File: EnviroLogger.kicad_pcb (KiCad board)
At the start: 2 copper layers, 100 x 99.5 mm, 30 parts, among them J3 Conn_01x03_Male, J4 Conn_01x02_Male, J5 Conn_01x02_Male, M1 RobotDyn_Li-Ion_Charger_W-Pro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, M2 MT3608_Boost_Regulator, M3 RobotDyn_MicroSD_Card_Reader, Q1 BSS138, Q2 BSS138, Q3 BSS138, SW1 SW_SPST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

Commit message: Updated to V1.1.0
Fixed many issues:
- Battery polarity was reversed
- I2C SDA and SCL were on the wrong Nano pins
- Added missing pull-up resistor on 5V side of I2C level shifter
- Added a real time clock to the design
- Fixed boost regulator wiring
- Changed MQ-135 control MOSFET to a part with much lower Rds(on) value.
The original part was dropping almost 25% as much voltage as the sensor
itself.
- Changed MQ-135 control to low-side switch design
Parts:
- removed J4, J5: Conn_01x02_Male, Connector_JST:JST_PH_S2B-PH-K_1x02_P2.00mm_Horizontal
- added BT1: Battery_Cell, Battery:BatteryHolder_Keystone_3000_1x12mm, F.Cu at (104.2, 132.5)
- added J1: Conn_01x02_Male, Connector_JST:JST_PH_S2B-PH-K_1x02_P2.00mm_Horizontal, F.Cu at (82.5, 112.5)
- added J2: Conn_01x02_Male, Connector_JST:JST_PH_S2B-PH-K_1x02_P2.00mm_Horizontal, F.Cu at (90.0, 112.5)
- added R10: 10k, Resistor_THT:R_Axial_DIN0207_L6.3mm_D2.5mm_P7.62mm_Horizontal, F.Cu at (43.5, 147.5)
- added R8: 10k, Resistor_THT:R_Axial_DIN0207_L6.3mm_D2.5mm_P7.62mm_Horizontal, F.Cu at (49.5, 147.5)
- added R9: 10k, Resistor_THT:R_Axial_DIN0207_L6.3mm_D2.5mm_P7.62mm_Horizontal, F.Cu at (46.5, 147.5)
- added U4: DS1307ZN+, Package_SO:SOIC-8_3.9x4.9mm_P1.27mm, F.Cu at (85.0, 163.8)
- added Y1: Crystal_GND23, Crystal:Crystal_SMD_CardinalComponents_CPFB-4Pin_8.7x3.7mm, F.Cu at (76.0, 163.8)
- Q1: value BSS138 -> DMN6140L
- R1: value 100k -> 100
- R2: value 8.25k -> 8.25k : 1%
- moved G*** 47.6 mm to (64.2, 120.5), turned to 0 degrees
- moved R7 15.4 mm to (109.2, 117.5), turned to 180 degrees
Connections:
- A1 pad 20: BUTTON_1 -> MQ-150_OUT
- A1 pad 21: BUTTON_2 -> MQ-135_OVERRIDE
- A1 pad 22: MQ-135_OVERRIDE -> LIGHT_SENSE_CURRENT
- A1 pad 23: LIGHT_SENSE_CURRENT -> SDA_5V
- A1 pad 24: MQ-150_OUT -> SCK_5V
- A1 pad 7: SDA_5V -> BUTTON_1
- A1 pad 8: SCK_5V -> BUTTON_2
- M1 pad 8: BATT+ -> BATT-
- M1 pad 9: BATT- -> BATT+
- Q1 pad 1: MQ-150_Toggle -> Net-(Q1-Pad1)
- Q1 pad 2: Net-(Q1-Pad2) -> GND
- Q1 pad 3: +5V -> Net-(Q1-Pad3)
- R1 pad 1: Net-(Q1-Pad2) -> Net-(Q1-Pad1)
- R1 pad 2: GND -> MQ-150_Toggle
- U2 pad 2: Net-(Q1-Pad2) -> +5V
- U2 pad 5: GND -> Net-(Q1-Pad3)
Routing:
- net Net-(Q1-Pad2): track 118.4 -> 0.00 mm
- net Net-(Q1-Pad3): track 0.00 -> 83.0 mm
- net Net-(BT1-Pad1): track 0.00 -> 63.8 mm, vias 0 -> 2
- net SDA_5V: track 36.1 -> 99.2 mm, vias 0 -> 3
- net SCK_5V: track 35.1 -> 93.2 mm, vias 0 -> 3
- net GND: track 14.7 -> 55.6 mm, vias 3 -> 4
- net MQ-150_Toggle: track 36.0 -> 65.4 mm, vias 0 -> 4
- net MQ-135_OVERRIDE: track 146.6 -> 125.4 mm
- net Net-(Q1-Pad1): track 0.00 -> 20.0 mm
- net BUTTON_1: track 66.5 -> 49.1 mm, vias 0 -> 2
- net INDICATOR_LED: track 129.7 -> 114.6 mm
- net +5V: track 106.7 -> 121.6 mm, vias 8 -> 7
- net MQ-150_OUT: track 116.6 -> 128.8 mm
- net +3V3: track 127.7 -> 139.4 mm, vias 4 -> 5
- net BUTTON_2: track 72.4 -> 63.9 mm, vias 0 -> 2
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- added copper zone on F.Cu, net GND
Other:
- board text added: "RTC BATTERY"
- board text added: "TinkerTech EnviroLogger - V1.0.1 11/13/18 User Manual: www.tinkertech.io/envirologger"
- board text removed: "4.7k"
- board text removed: "TinkerTech EnviroLogger - V1.0.0 10/30/18 User Manual: www.tinkertech.io/envirologger"

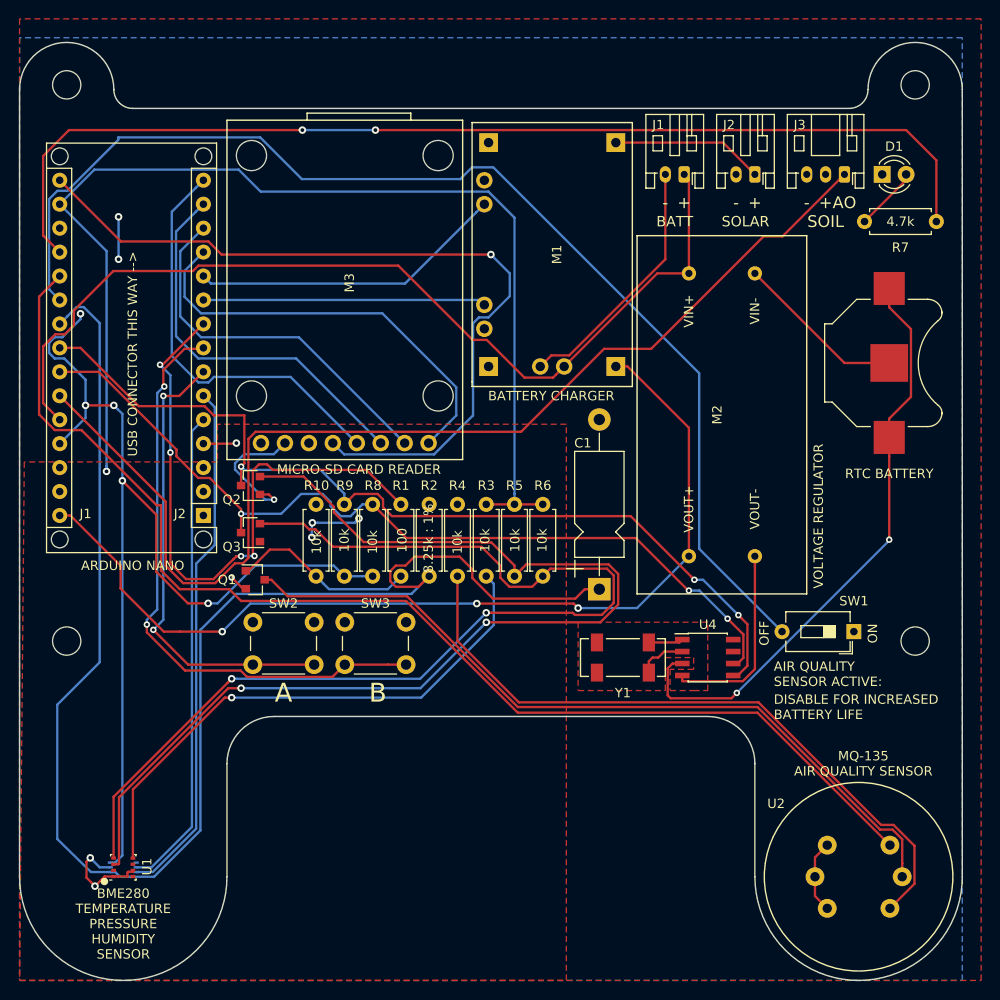
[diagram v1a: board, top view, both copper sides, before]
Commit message: Update to V1.0.2
Fixed battery grounding issue
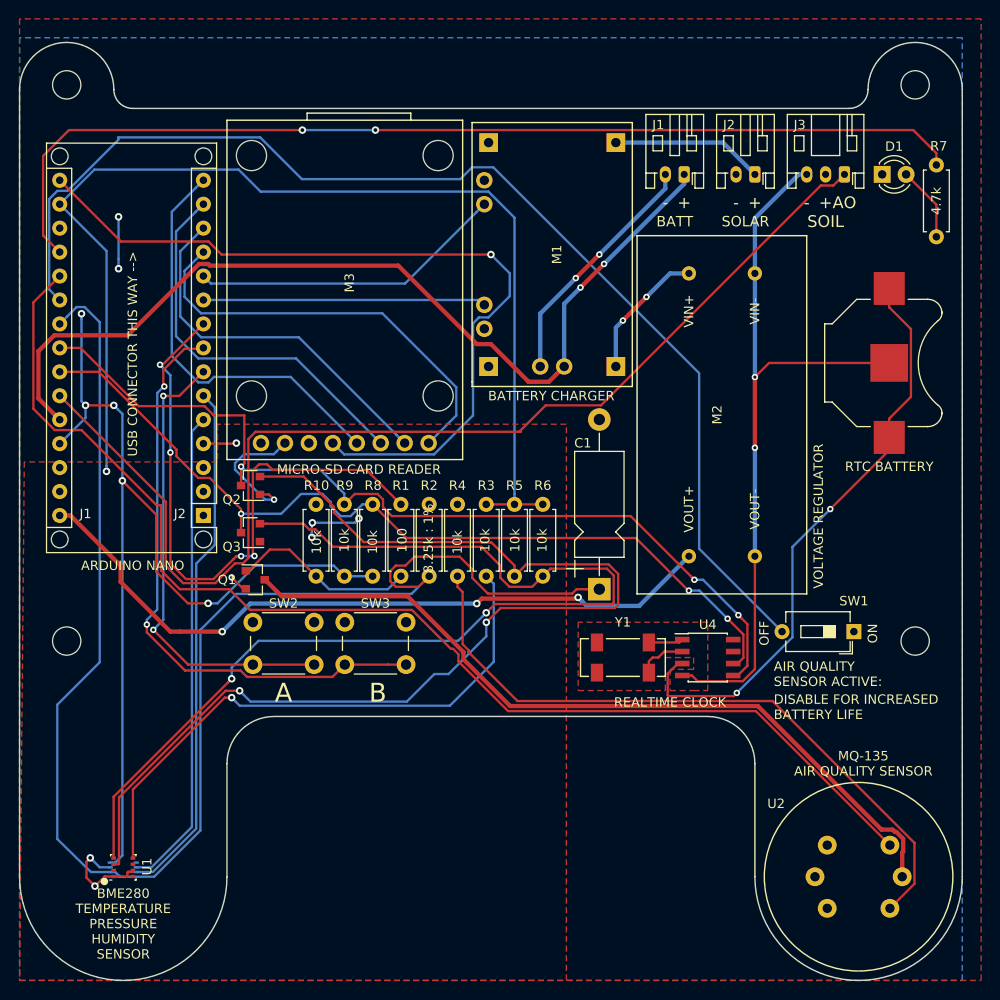
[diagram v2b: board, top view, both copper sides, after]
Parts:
- removed G***: LOGO, Symbol:TinkerTech-Logo_51.6x15mm_SilkScreen
- added SLK1: TT_Logo, Symbol:TinkerTech-Logo_34.4x10mm_SilkScreen, B.Cu at (100.5, 139.0)
- moved R7 6.00 mm to (109.2, 111.5), turned to 270 degrees
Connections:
- net Net-(Q1-Pad3) renamed MQ-150-GND
- J1 pad 2: BATT- -> GND
- M1 pad 10: NANO_VIN -> CHARGER_VOUT
- M1 pad 8: BATT- -> GND
- M2 pad 4: BATT+ -> CHARGER_VOUT
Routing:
- net GND: track 55.6 -> 121.1 mm, vias 4 -> 8
- net BATT-: track 27.0 -> 0.00 mm
- net NANO_VIN: track 101.0 -> 76.9 mm
- net CHARGER_VOUT: track 0.00 -> 14.3 mm, vias 0 -> 2
- net +5V: track 121.6 -> 110.9 mm
- net INDICATOR_LED: track 114.6 -> 109.1 mm
- net Net-(R3-Pad2): track 58.3 -> 61.3 mm
- net BATT+: track 101.7 -> 99.3 mm, vias 0 -> 2
- net SDA_3.3V: track 116.6 -> 118.4 mm
- net Net-(D1-Pad2): track 6.83 -> 8.54 mm
- net MQ-150_OUT: track 128.8 -> 129.8 mm
- net MQ-150-GND: track 83.0 -> 83.6 mm
- net Net-(BT1-Pad1): track 63.8 -> 63.3 mm
- net SCK_3.3V: track 113.3 -> 113.8 mm
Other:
- net class Power added: clearance 0.1778, trace_width 0.459, via_dia 0.6858, via_drill 0.3302
- board text added: "REALTIME CLOCK"
- board text added: "TinkerTech EnviroLogger - V1.0.2 12/4/18 User Manual: www.tinkertech.io/envirologger"
- board text removed: "TinkerTech EnviroLogger - V1.0.1 11/13/18 User Manual: www.tinkertech.io/envirologger"

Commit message: Updated to V1.1.0
Added solar charging circuitry
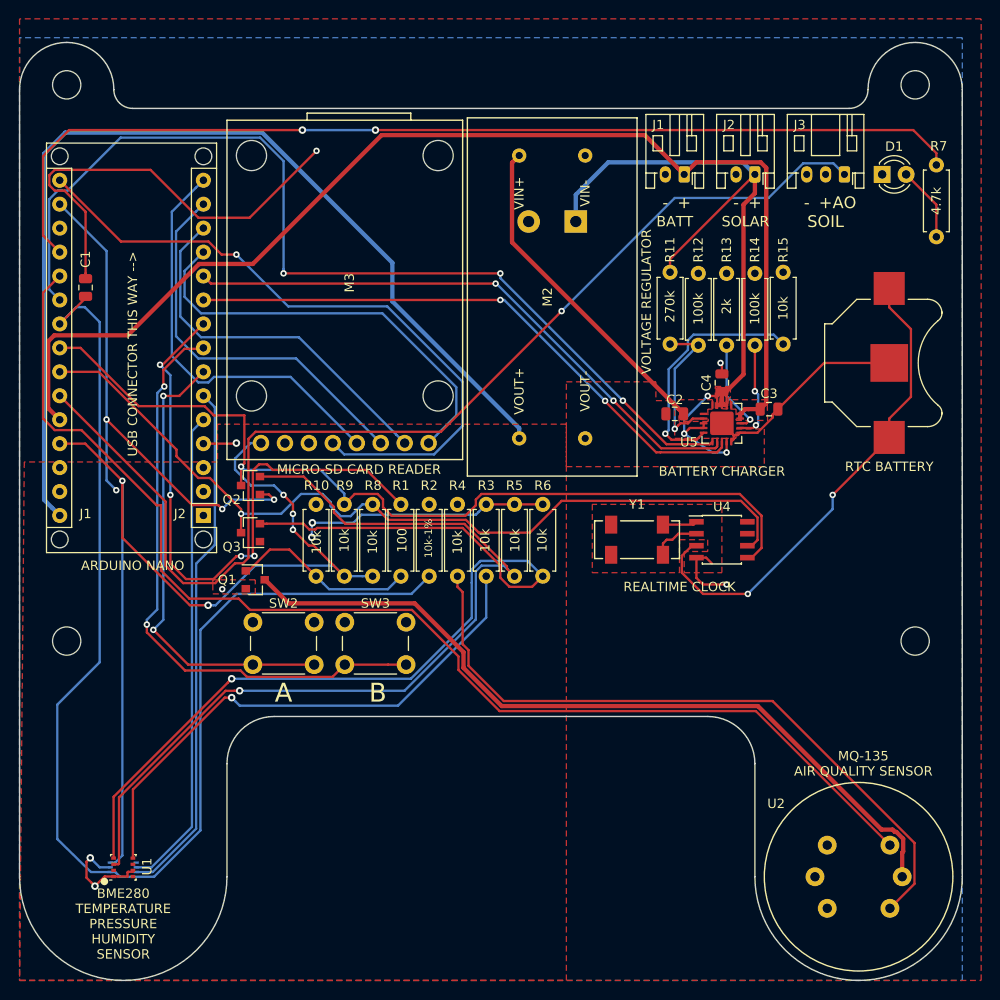
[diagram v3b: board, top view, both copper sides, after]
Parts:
- removed M1: RobotDyn_Li-Ion_Charger_W-Protection, TT_Module:RobotDyn_Li-Ion_Charger_W-Protection
- removed SW1: SW_SPST, Button_Switch_THT:SW_DIP_SPSTx01_Slide_6.7x4.1mm_W7.62mm_P2.54mm_LowProfile
- added C2: 10uF, Capacitor_SMD:C_0805_2012Metric, F.Cu at (81.5, 137.9)
- added C3: 10uF, Capacitor_SMD:C_0805_2012Metric, F.Cu at (91.5, 137.4)
- added C4: 10uF, Capacitor_SMD:C_0805_2012Metric, F.Cu at (86.5, 134.6)
- added C5: 4700uF, Capacitor_THT:CP_Radial_D12.5mm_P5.00mm, B.Cu at (71.0, 117.5)
- added R11: 270k, Resistor_THT:R_Axial_DIN0207_L6.3mm_D2.5mm_P7.62mm_Horizontal, F.Cu at (81.0, 130.5)
- added R12: 100k, Resistor_THT:R_Axial_DIN0207_L6.3mm_D2.5mm_P7.62mm_Horizontal, F.Cu at (84.0, 123.0)
- added R13: 2k, Resistor_THT:R_Axial_DIN0207_L6.3mm_D2.5mm_P7.62mm_Horizontal, F.Cu at (87.0, 123.0)
- added R14: 100k, Resistor_THT:R_Axial_DIN0207_L6.3mm_D2.5mm_P7.62mm_Horizontal, F.Cu at (90.0, 123.0)
- added R15: 10k, Resistor_THT:R_Axial_DIN0207_L6.3mm_D2.5mm_P7.62mm_Horizontal, F.Cu at (93.0, 130.5)
- added U5: MCP73871, Package_DFN_QFN:QFN-20-1EP_4x4mm_P0.5mm_EP2.5x2.5mm, F.Cu at (86.5, 138.9)
- C1: value 12uF -> 10uF; footprint Capacitor_THT:CP_Axial_L11.0mm_D5.0mm_P18.00mm_Horizontal -> Capacitor_SMD:C_0805_2012Metric
- R2: value 8.25k : 1% -> 10k-1%
- moved C1 63.2 mm to (19.0, 124.5)
- moved M2 21.9 mm to (68.5, 125.5)
- moved U4 12.6 mm to (86.5, 151.2)
- moved Y1 12.6 mm to (77.5, 151.2)
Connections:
- A1 pad 10: CHG_ACTIVE -> STAT1
- A1 pad 11: CHG_STBY -> STAT2
- A1 pad 21: MQ-135_OVERRIDE -> ~PG
- M3 pad 7: +3V3 -> Net-(M3-Pad7)
- M3 pad 8: Net-(M3-Pad8) -> +5V
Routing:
- net MQ-135_OVERRIDE: track 125.4 -> 0.00 mm
- net ~PG: track 0.00 -> 105.1 mm, vias 0 -> 3
- net SOLAR+: track 16.1 -> 85.9 mm, vias 0 -> 3
- net STAT2: track 0.00 -> 62.7 mm, vias 0 -> 2
- net STAT1: track 0.00 -> 62.6 mm, vias 0 -> 2
- net +3V3: track 139.4 -> 83.5 mm, vias 5 -> 6
- net CHG_STBY: track 33.6 -> 0.00 mm
- net CHG_ACTIVE: track 30.0 -> 0.00 mm
- net NANO_VIN: track 76.9 -> 106.8 mm, vias 3 -> 0
- net GND: track 121.1 -> 92.9 mm, vias 8 -> 7
- net LIGHT_SENSE_CURRENT: track 160.2 -> 133.1 mm
- net Net-(R15-Pad1): track 0.00 -> 26.3 mm, vias 0 -> 1
- net BATT+: track 99.3 -> 125.2 mm, vias 2 -> 0
- net SDA_3.3V: track 118.4 -> 95.1 mm, vias 2 -> 1
- net CHARGER_VOUT: track 14.3 -> 35.3 mm, vias 2 -> 0
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- added copper zone on F.Cu, net BATT+
- added copper zone on F.Cu, net CHARGER_VOUT
- added copper zone on F.Cu, net SOLAR+
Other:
- board text added: "TinkerTech EnviroLogger - V1.1.0 12/5/18 User Manual: www.tinkertech.io/envirologger"
- board text removed: "AIR QUALITY SENSOR ACTIVE:"
- board text removed: "DISABLE FOR INCREASED BATTERY LIFE"
- board text removed: "OFF"
- board text removed: "ON"
- board text removed: "TinkerTech EnviroLogger - V1.0.2 12/4/18 User Manual: www.tinkertech.io/envirologger"
